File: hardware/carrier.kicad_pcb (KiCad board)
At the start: 2 copper layers, 90 x 60 mm, 49 parts, among them J2 Heltec_J2, J3 Heltec_J3, U1 MT3608

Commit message: hardware: boost loop placement, solid GND pour, review cleanup
Co-Authored-By: Claude Opus 5.5 <noreply@anthropic.com>
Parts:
- moved C_OUT1 16.6 mm to (21.0, 20.0)
- moved C_OUT2 16.4 mm to (21.0, 22.9)
- moved D1 9.20 mm to (21.3, 16.0), turned to 0 degrees
- moved L1 6.02 mm to (28.5, 15.5), turned to 180 degrees
- moved R_FB2 4.24 mm to (26.5, 25.5), turned to 0 degrees
- moved C_IN1 1.89 mm to (31.2, 21.8), turned to 90 degrees
- moved R_FB1 1.50 mm to (22.0, 26.0)
- moved U1 1.04 mm to (27.0, 21.5)
- moved F1 0.30 mm to (15.2, 14.0)

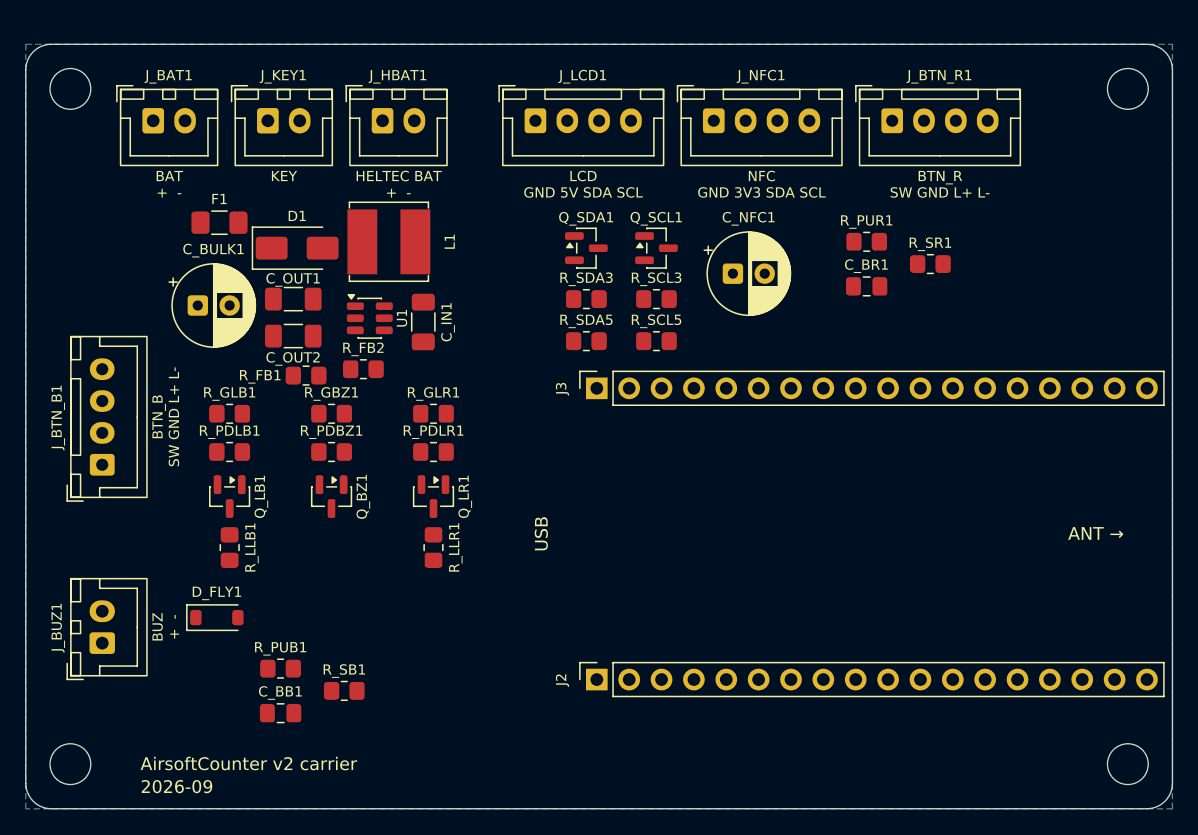
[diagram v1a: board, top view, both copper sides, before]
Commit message: hardware: autorouted board, DRC clean
route.py exports DSN, runs Freerouting 2.4.1 headless, imports the SES,
adds a GND pour on F.Cu and fills zones. Refuses an already-routed board
(re-run gen_pcb.py first). Output is byte-identical across runs.

Co-Authored-By: Claude Opus 5.5 <noreply@anthropic.com>
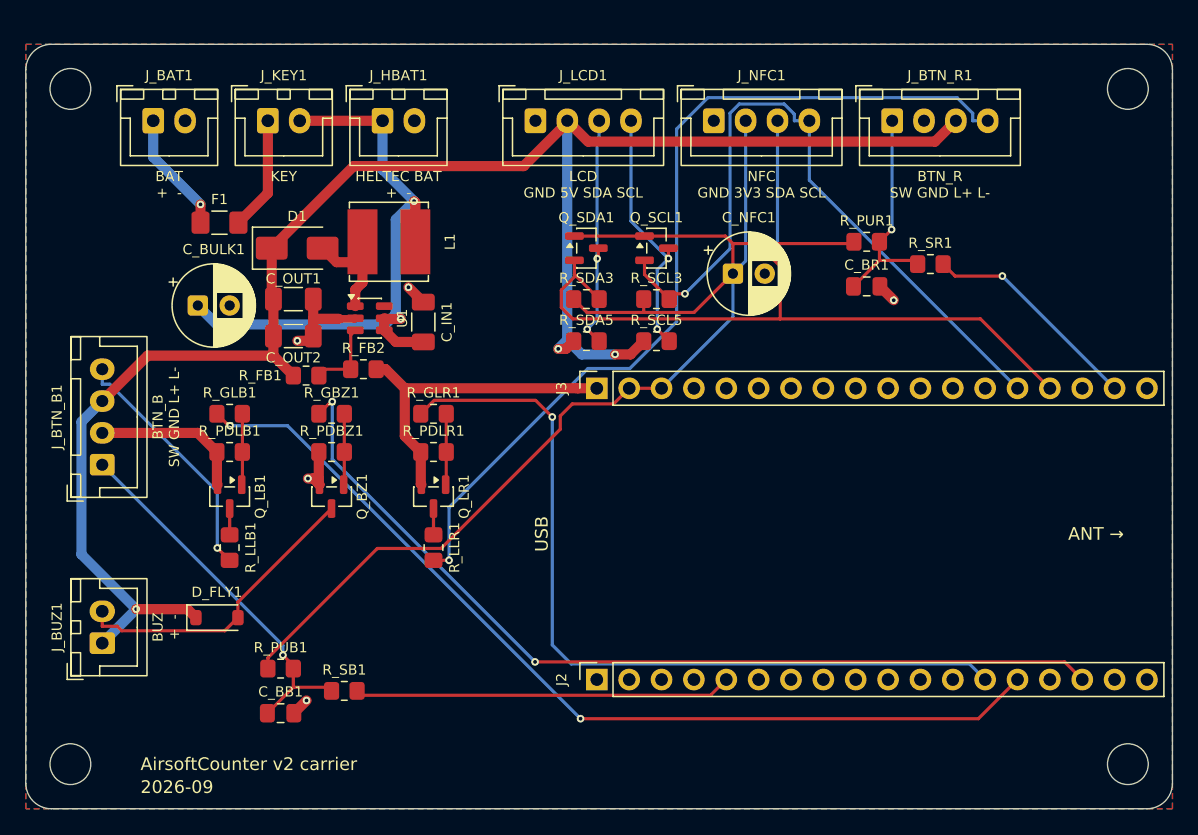
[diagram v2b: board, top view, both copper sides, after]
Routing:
- net +5V: track 0.00 -> 138.9 mm, vias 0 -> 3
- net +3V3: track 0.00 -> 104.7 mm
- net LED_B_G: track 0.00 -> 74.0 mm, vias 0 -> 2
- net BUZ_G: track 0.00 -> 72.0 mm, vias 0 -> 2
- net BTN_R_LEDK: track 0.00 -> 70.9 mm, vias 0 -> 1
- net LED_R_G: track 0.00 -> 64.3 mm, vias 0 -> 1
- net SDA_3V3: track 0.00 -> 64.1 mm, vias 0 -> 1
- net SCL_3V3: track 0.00 -> 56.0 mm, vias 0 -> 1
- net GND: track 0.00 -> 54.2 mm, vias 0 -> 5
- net VBAT_SW: track 0.00 -> 49.3 mm, vias 0 -> 2
- net BTN_B_SW: track 0.00 -> 29.7 mm, vias 0 -> 1
- net BTN_B_IN: track 0.00 -> 29.6 mm
- net BUZ_K: track 0.00 -> 24.0 mm
- net SCL_5V: track 0.00 -> 20.1 mm, vias 0 -> 2
- net BTN_B_LEDK: track 0.00 -> 19.5 mm, vias 0 -> 1
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- added copper zone on F.Cu, net GND

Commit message: hardware: C_IN1 rotation, silk stroke, route.py review fixes
C_IN1 at 270 deg puts its VBAT_SW pad next to L1.1: VBAT_SW routes via-free
on F.Cu. Silk stroke 0.15 mm minimum. Zone island removal set explicitly.
route.py: missing java and a missing GND pour exit cleanly; note that the
unrouted-count regex follows Freerouting 2.4.1 log wording.

Co-Authored-By: Claude Opus 5.5 <noreply@anthropic.com>
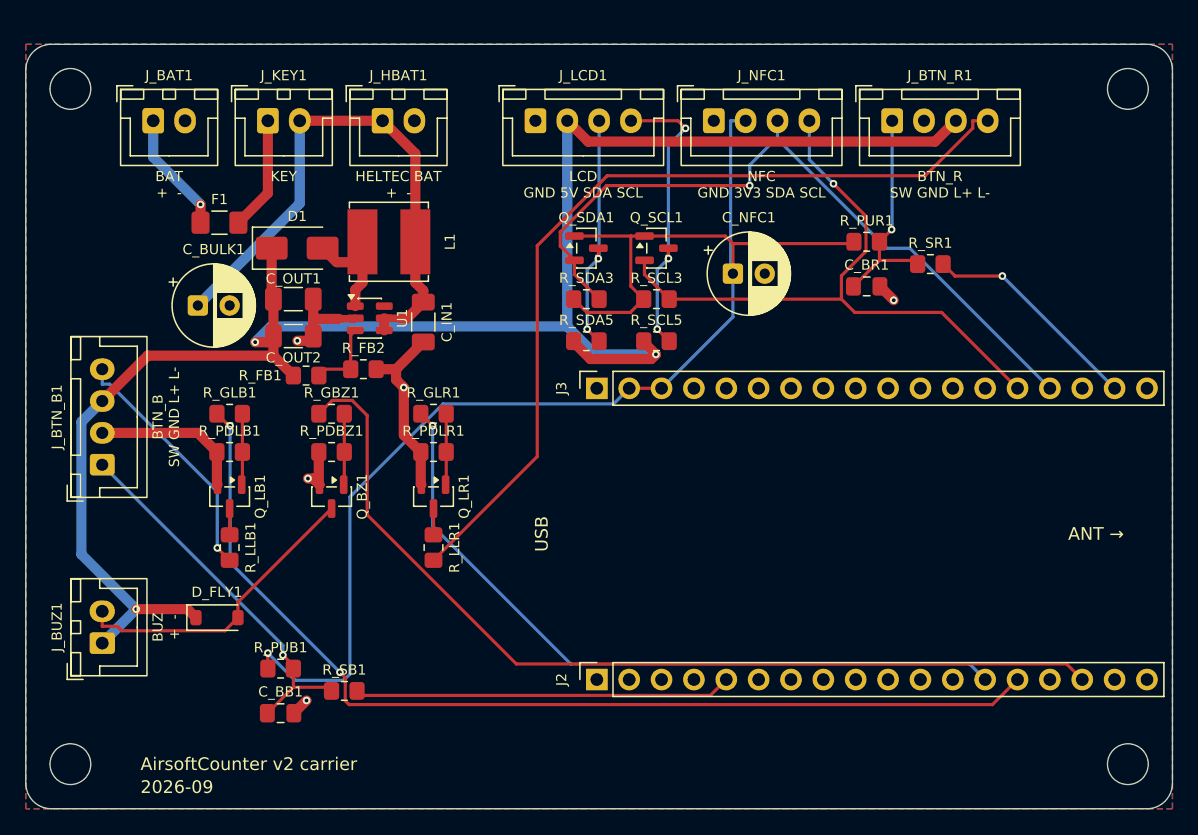
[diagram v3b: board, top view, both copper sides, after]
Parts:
- turned C_IN1 to -90 degrees
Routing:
- net GND: track 54.2 -> 40.9 mm
- net +3V3: track 104.7 -> 111.5 mm, vias 0 -> 1
- net LED_R_G: track 64.3 -> 57.5 mm
- net LED_B_G: track 74.0 -> 80.5 mm
- net SDA_3V3: track 64.1 -> 58.5 mm
- net +5V: track 138.9 -> 144.3 mm
- net SCL_3V3: track 56.0 -> 50.7 mm
- net VBAT_SW: track 49.3 -> 44.4 mm, vias 2 -> 0
- net SCL_5V: track 20.1 -> 23.4 mm, vias 2 -> 3
- net BTN_R_LEDK: track 70.9 -> 67.8 mm, vias 1 -> 0
- net BUZ_G: track 72.0 -> 74.0 mm, vias 2 -> 0

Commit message: hardware: JLCPCB assembly BOM + CPL (full SMD+THT)
design.py: LCSC map keyed by (value, footprint); check() fails if an
assembled part (not DNP, not a mounting hole) has no LCSC number or an
entry is unused. Part numbers verified live against JLCPCB's parts API
on 2026-09-29. Cap values now state the picked parts' ratings:
22uF 25V, 220uF 16V, 100uF 25V.

jlc.py (run by make fab) writes fab/jlc_bom.csv and fab/jlc_cpl.csv from
design.py and kicad-cli's pos export, and checks: BOM and CPL designators
match exactly once, every row has an LCSC number, the pos anchors equal
the board coordinates with Y negated (the Gerber convention), and every
placement lies inside the Gerber Edge.Cuts extent. Mid X/Y is the pad
centre, because THT footprints are anchored on pin 1. No rotation
offsets: ORDERING.md lists the parts to check in JLC's 3D preview.

ORDERING.md: Economic PCBA section (upload steps, THT, setup-fee types,
preview checks, stock and backups).

Co-Authored-By: Claude Opus 5.5 <noreply@anthropic.com>
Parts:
- C_BULK1: value 220uF 10V -> 220uF 16V
- C_IN1, C_OUT1, C_OUT2: value 22uF 10V -> 22uF 25V
- C_NFC1: value 100uF 10V -> 100uF 25V
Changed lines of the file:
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@@
 			)
 		)
-		(property "Value" "220uF 10V"
+		(property "Value" "220uF 16V"
 			(at 1.25 4.4 0)
 			(layer "F.Fab")
@@
 			)
 		)
-		(property "Value" "22uF 10V"
+		(property "Value" "22uF 25V"
 			(at 0 1.85 0)
 			(layer "F.Fab")
@@
 			)
 		)
-		(property "Value" "22uF 10V"
+		(property "Value" "22uF 25V"
 			(at 0 1.85 0)
 			(layer "F.Fab")
@@
 			)
 		)
-		(property "Value" "22uF 10V"
+		(property "Value" "22uF 25V"
 			(at 0 1.85 270)
 			(layer "F.Fab")
@@
 			)
 		)
-		(property "Value" "100uF 10V"
+		(property "Value" "100uF 25V"
 			(at 1.25 4.4 0)
 			(layer "F.Fab")

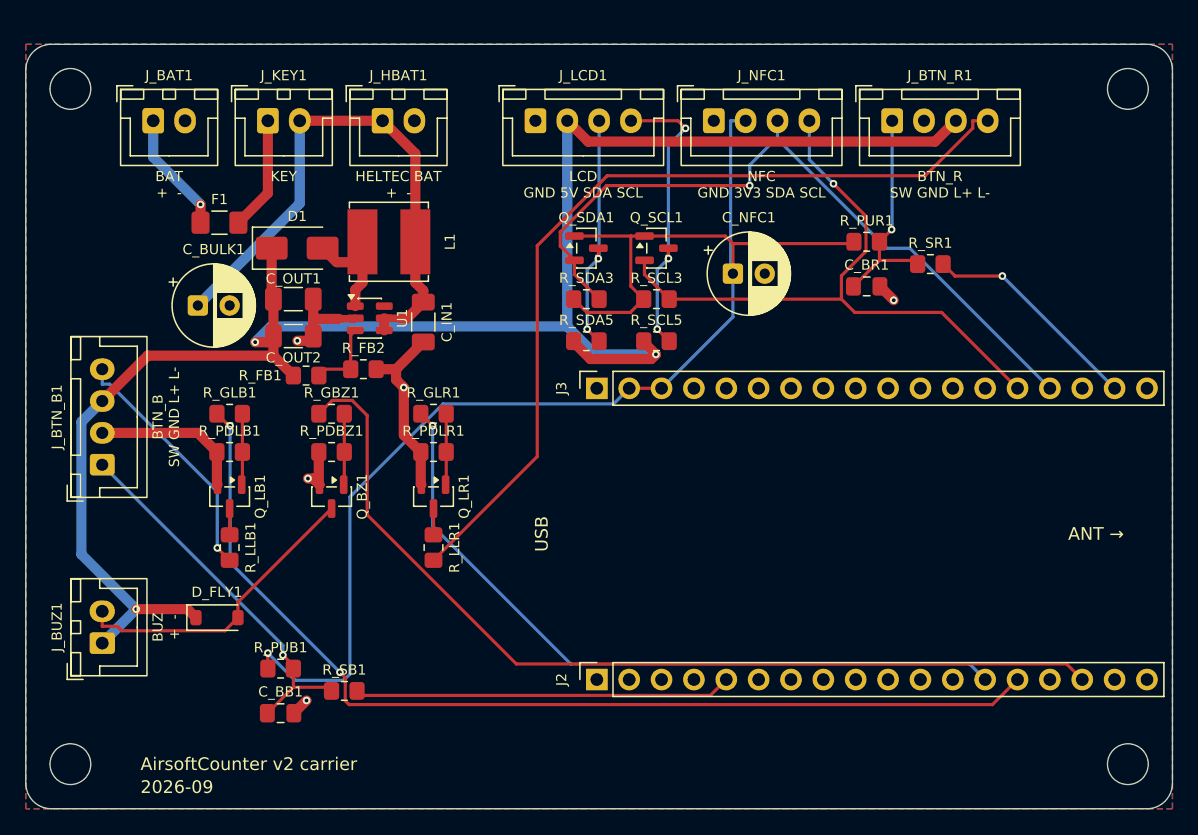
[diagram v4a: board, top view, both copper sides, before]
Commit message: hardware: I2S speaker amp, TCA9534 expander, ceramic bulk caps
Task A10 (design Part 6):
- U2 TCA9534PWR (C783615) at 0x20 on the 3V3 I2C bus, INT on GPIO6
  (R_INT1 10k): buttons on P0/P1, LED/buzzer gate drives on P2-P4,
  amp SD_MODE on P5 (through R_SD1 1k, datasheet abs-max guidance).
- U3 MAX98357AETE+T (C910544) on VBAT_SW, I2S on GPIO47/48/21, 12 dB,
  BTL output to J_SPK1 (pin 1 OUT-, silk "SPK (BTL, not GND)").
- THT 220uF/100uF -> 2x 47uF 10V (C96123) + 100uF 6.3V (C15008) 1206
  Basic ceramics; F1 -> 2A PTC 1206L200/16NR (C22374899).
- R_LLR1/R_LLB1 -> 0R (C17477): ONPOW 6V button LEDs have a resistor.
- GND leaves the Power net class, Power clearance 0.2 mm, board min
  track 0.15 mm (Freerouting necks into the fine-pitch pads); U3
  thermal vias widened to 0.3 mm; ERC treats Unspecified as Passive.
LCSC numbers verified live 2026-09-29. ERC 0, DRC 0/0/0 at all
severities, 23 JLC BOM lines, 52 placements, deterministic rebuild.

Co-Authored-By: Claude Opus 5.5 <noreply@anthropic.com>
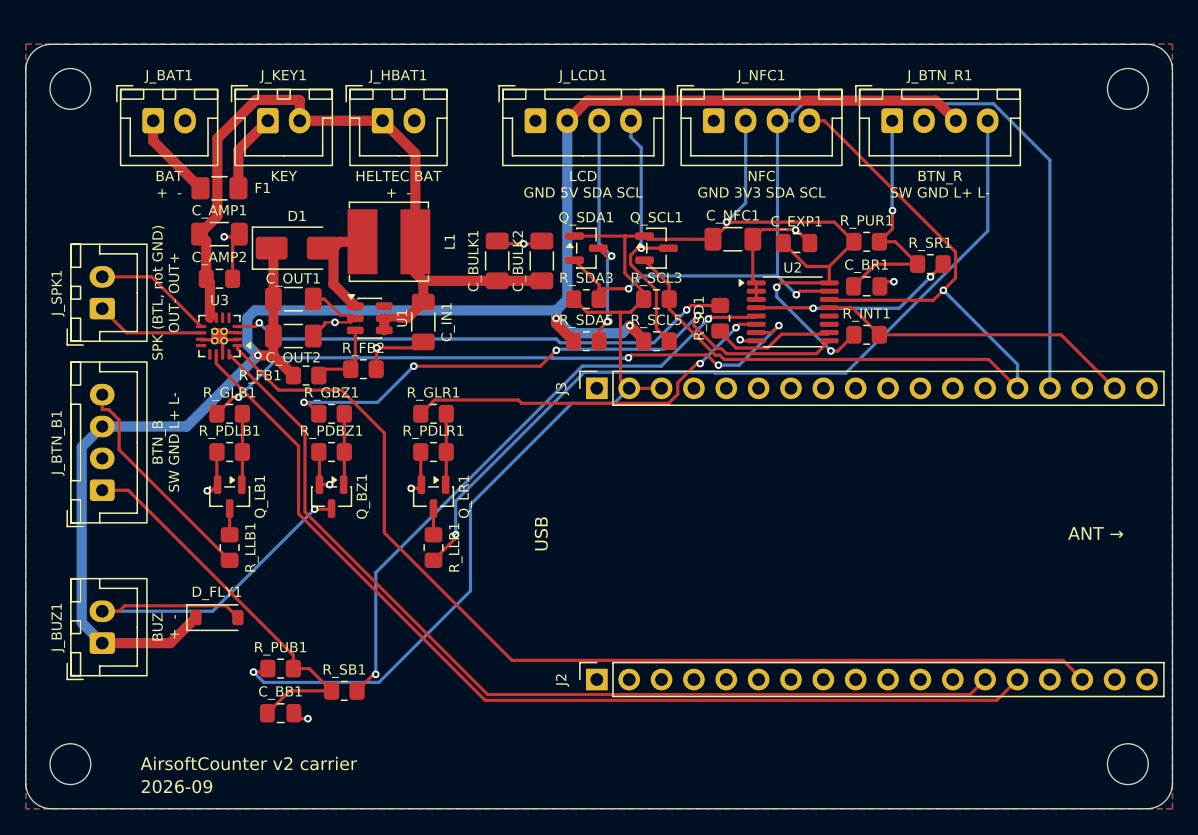
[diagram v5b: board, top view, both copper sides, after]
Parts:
- added C_AMP1: 22uF 25V, Capacitor_SMD:C_1206_3216Metric_Pad1.33x1.80mm_HandSolder, F.Cu at (15.2, 14.9)
- added C_AMP2: 100nF, Capacitor_SMD:C_0805_2012Metric_Pad1.18x1.45mm_HandSolder, F.Cu at (15.2, 18.4)
- added C_BULK2: 47uF 10V, Capacitor_SMD:C_1206_3216Metric_Pad1.33x1.80mm_HandSolder, F.Cu at (40.5, 17.0)
- added C_EXP1: 100nF, Capacitor_SMD:C_0805_2012Metric_Pad1.18x1.45mm_HandSolder, F.Cu at (60.5, 15.6)
- added J_SPK1: SPK, Connector_JST:JST_XH_B2B-XH-A_1x02_P2.50mm_Vertical, F.Cu at (6.00, 20.8)
- added R_INT1: 10k, Resistor_SMD:R_0805_2012Metric_Pad1.20x1.40mm_HandSolder, F.Cu at (66.0, 22.8)
- added R_SD1: 1k, Resistor_SMD:R_0805_2012Metric_Pad1.20x1.40mm_HandSolder, F.Cu at (54.5, 21.5)
- added U2: TCA9534PWR, Package_SO:TSSOP-16_4.4x5mm_P0.65mm, F.Cu at (60.2, 21.0)
- added U3: MAX98357A, Package_DFN_QFN:TQFN-16-1EP_3x3mm_P0.5mm_EP1.23x1.23mm_ThermalVias, F.Cu at (15.2, 22.9)
- C_BULK1: value 220uF 16V -> 47uF 10V; footprint Capacitor_THT:CP_Radial_D6.3mm_P2.50mm -> Capacitor_SMD:C_1206_3216Metric_Pad1.33x1.80mm_HandSolder
- C_NFC1: value 100uF 25V -> 100uF 6.3V; footprint Capacitor_THT:CP_Radial_D6.3mm_P2.50mm -> Capacitor_SMD:C_1206_3216Metric_Pad1.33x1.80mm_HandSolder
- F1: value 1A PTC -> 2A PTC
- R_LLB1: value 100R -> 0R
- R_LLR1: value 150R -> 0R
- moved C_BULK1 23.8 mm to (37.0, 17.0), turned to 90 degrees
- moved C_NFC1 2.70 mm to (55.5, 15.3)
- moved F1 2.70 mm to (15.2, 11.3)
- moved J_BTN_B1 2.00 mm to (6.00, 35.0)
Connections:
- J2 pad 13: LED_R_G -> I2S_BCLK
- J2 pad 14: LED_B_G -> I2S_LRCLK
- J2 pad 16: BUZ_G -> I2S_DIN
- J2 pad 5: BTN_B_IN -> unconnected-(J2-Pin_5-Pad5)
- J3 pad 17: BTN_R_IN -> EXP_INT
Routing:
- net I2S_DIN: track 0.00 -> 81.9 mm
- net I2S_LRCLK: track 0.00 -> 78.4 mm
- net I2S_BCLK: track 0.00 -> 74.6 mm
- net AMP_SD_R: track 0.00 -> 39.8 mm, vias 0 -> 2
- net LED_B_G: track 80.5 -> 49.7 mm, vias 2 -> 4
- net LED_R_G: track 57.5 -> 30.0 mm, vias 1 -> 2
- net BUZ_G: track 74.0 -> 48.1 mm, vias 0 -> 4
- net EXP_INT: track 0.00 -> 25.0 mm
- net SCL_3V3: track 50.7 -> 73.1 mm
- net SDA_3V3: track 58.5 -> 77.2 mm, vias 1 -> 2
- net BTN_B_IN: track 29.6 -> 48.2 mm, vias 0 -> 2
- net VBAT_SW: track 44.4 -> 60.7 mm
- net GND: track 40.9 -> 51.4 mm, vias 5 -> 11
- net AMP_SD: track 0.00 -> 9.66 mm
- net SPK_P: track 0.00 -> 9.38 mm
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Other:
- board text added: "SPK (BTL, not GND) OUT- OUT+"

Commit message: hardware: amp GND vias, severity-all checks, review cleanup
- gen_pcb.py: locked GND vias tied to C_AMP1.2/C_AMP2.2 (amp
  decoupling returns to the B.Cu pour, 4.6 mm to U3's EP vias instead
  of a >20 mm F.Cu detour) and 3 stitching vias along the I2S corridor;
  via widening reuses gen_sch.VIA.
- route.py: keep locked tracks/vias (refuse only unlocked ones) and
  strip KiCad's GND plane from the DSN, so Freerouting routes GND
  instead of assuming an ideal B.Cu plane that its own traces cut
  (J3.1 had ended up islanded).
- Makefile: ERC/DRC with --severity-all.
- gen_sch.py: named PASSIVE/UNSPEC pin-map indices, assert U3.17 is
  the only Unspecified pin; shared VIA constant.
- design.py: footprint constants above PARTS and used there.
- Plan: I2S crossing/stitching note, GND routing note, low-battery
  brownout note for audio + LoRa TX.

Co-Authored-By: Claude Opus 5.5 <noreply@anthropic.com>
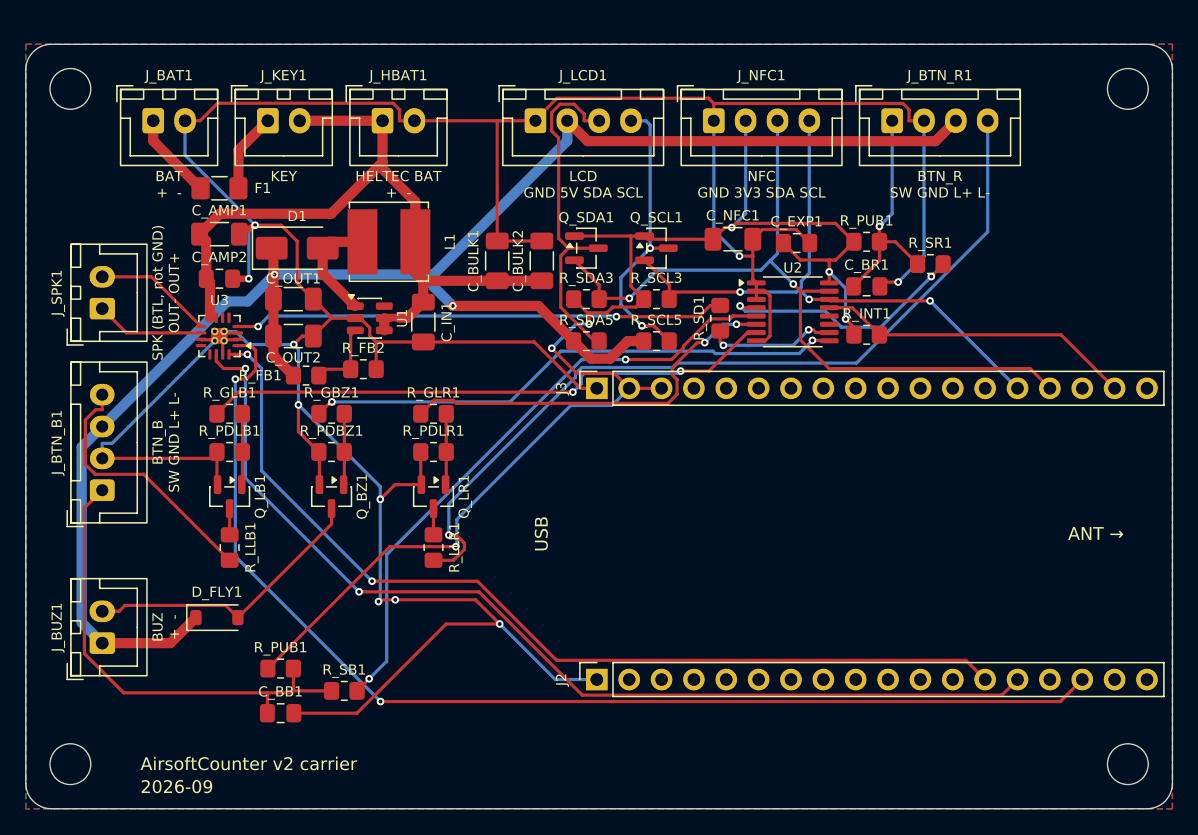
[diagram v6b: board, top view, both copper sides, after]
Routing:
- net GND: track 51.4 -> 290.7 mm, vias 11 -> 10
- net SCL_3V3: track 73.1 -> 48.1 mm, vias 1 -> 3
- net SDA_3V3: track 77.2 -> 60.3 mm
- net BUZ_K: track 32.6 -> 22.8 mm, vias 1 -> 0
- net I2S_DIN: track 81.9 -> 90.8 mm, vias 0 -> 2
- net SDA_5V: track 19.4 -> 27.4 mm, vias 2 -> 0
- net +3V3: track 119.0 -> 111.2 mm, vias 4 -> 6
- net BTN_B_SW: track 30.9 -> 37.5 mm
- net BUZ_G: track 48.1 -> 42.6 mm, vias 4 -> 2
- net LED_B_G: track 49.7 -> 45.3 mm, vias 4 -> 2
- net BTN_R_IN: track 16.1 -> 20.0 mm
- net BTN_B_LEDK: track 17.4 -> 20.8 mm
- net BTN_R_LEDK: track 64.6 -> 67.2 mm
- net +5V: track 139.0 -> 136.9 mm, vias 3 -> 2
- net SCL_5V: track 21.5 -> 23.1 mm, vias 1 -> 2
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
